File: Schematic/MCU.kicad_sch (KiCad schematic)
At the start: 2 parts, among them J4 Conn_02x20_Odd_Even, J5 Conn_02x20_Odd_Even

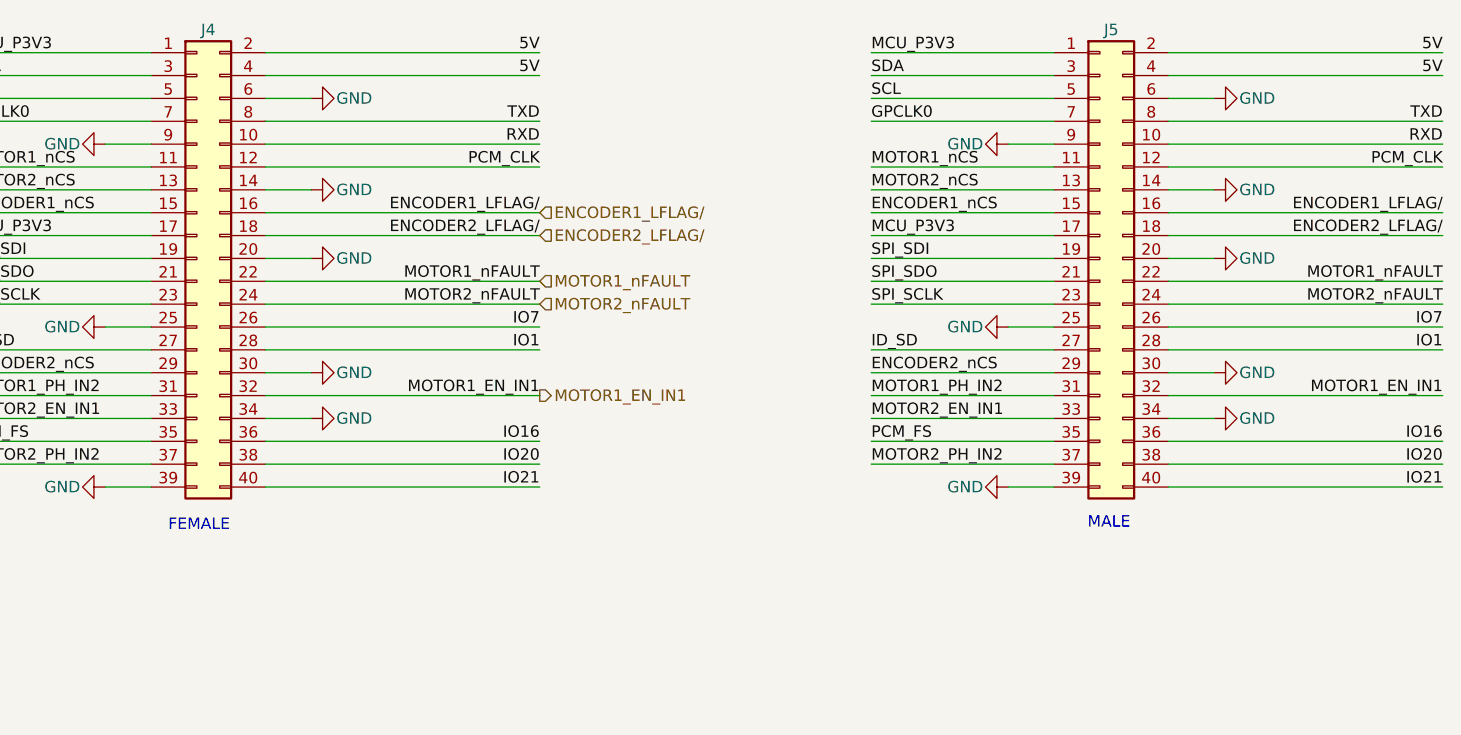
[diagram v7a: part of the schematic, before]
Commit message: Added fuse, more footprints, and cleaned up some things
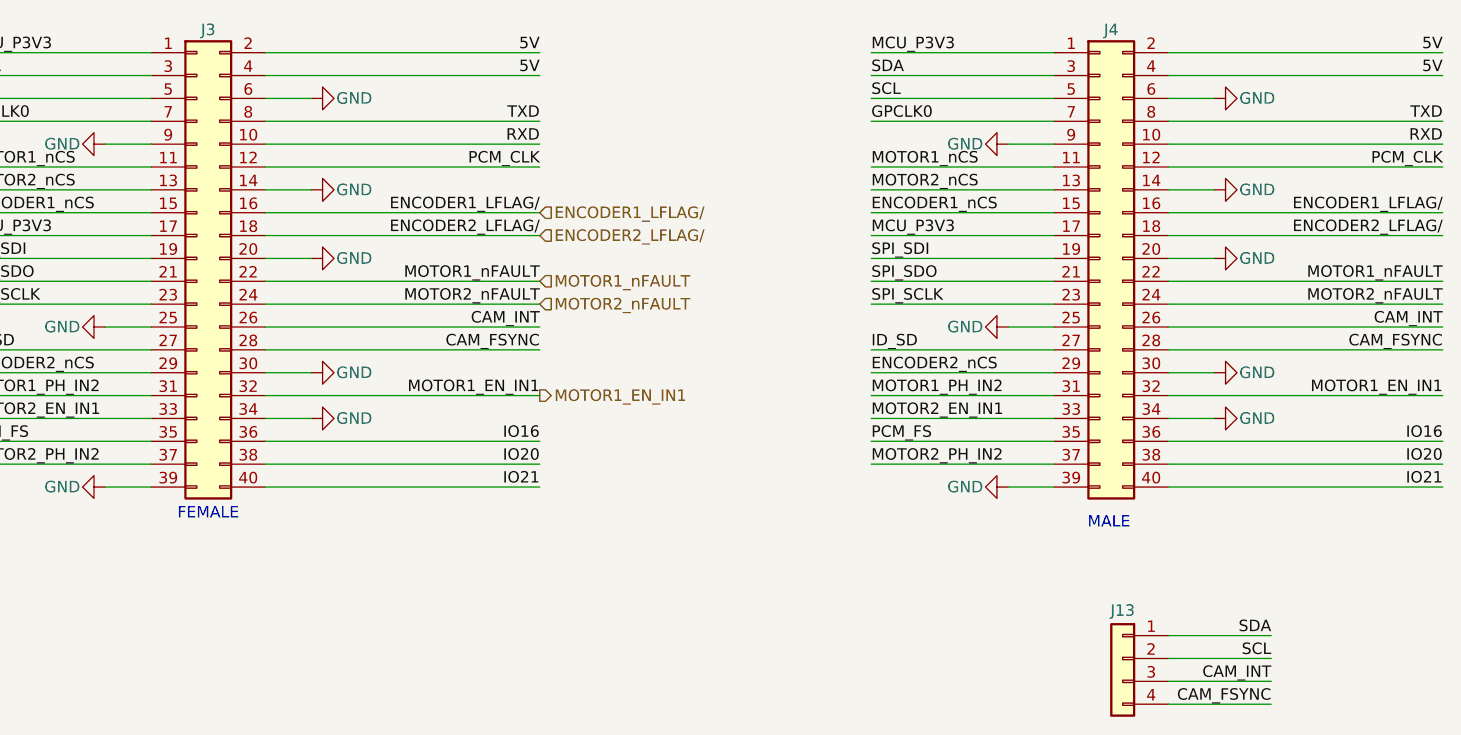
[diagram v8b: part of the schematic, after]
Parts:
- added J13: CAM, Connector_PinHeader_2.54mm:PinHeader_1x04_P2.54mm_Vertical, symbol Connector_Generic:Conn_01x04
- renumbered J4 to J3, J5 to J4
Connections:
- net SCL: now also J13.2 (Pin_2)
- net SDA: now also J13.1 (Pin_1)
- net IO1 renamed CAM_FSYNC
- net CAM_FSYNC: now also J13.4 (Pin_4)
- net IO7 renamed CAM_INT
- net CAM_INT: now also J13.3 (Pin_3)
